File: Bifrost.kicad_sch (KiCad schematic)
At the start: 59 parts, among them J1 OIP, J2 Conn_01x03_Male, J3 Conn_01x03_Male, U1 RLP-50, U3 LMH6881

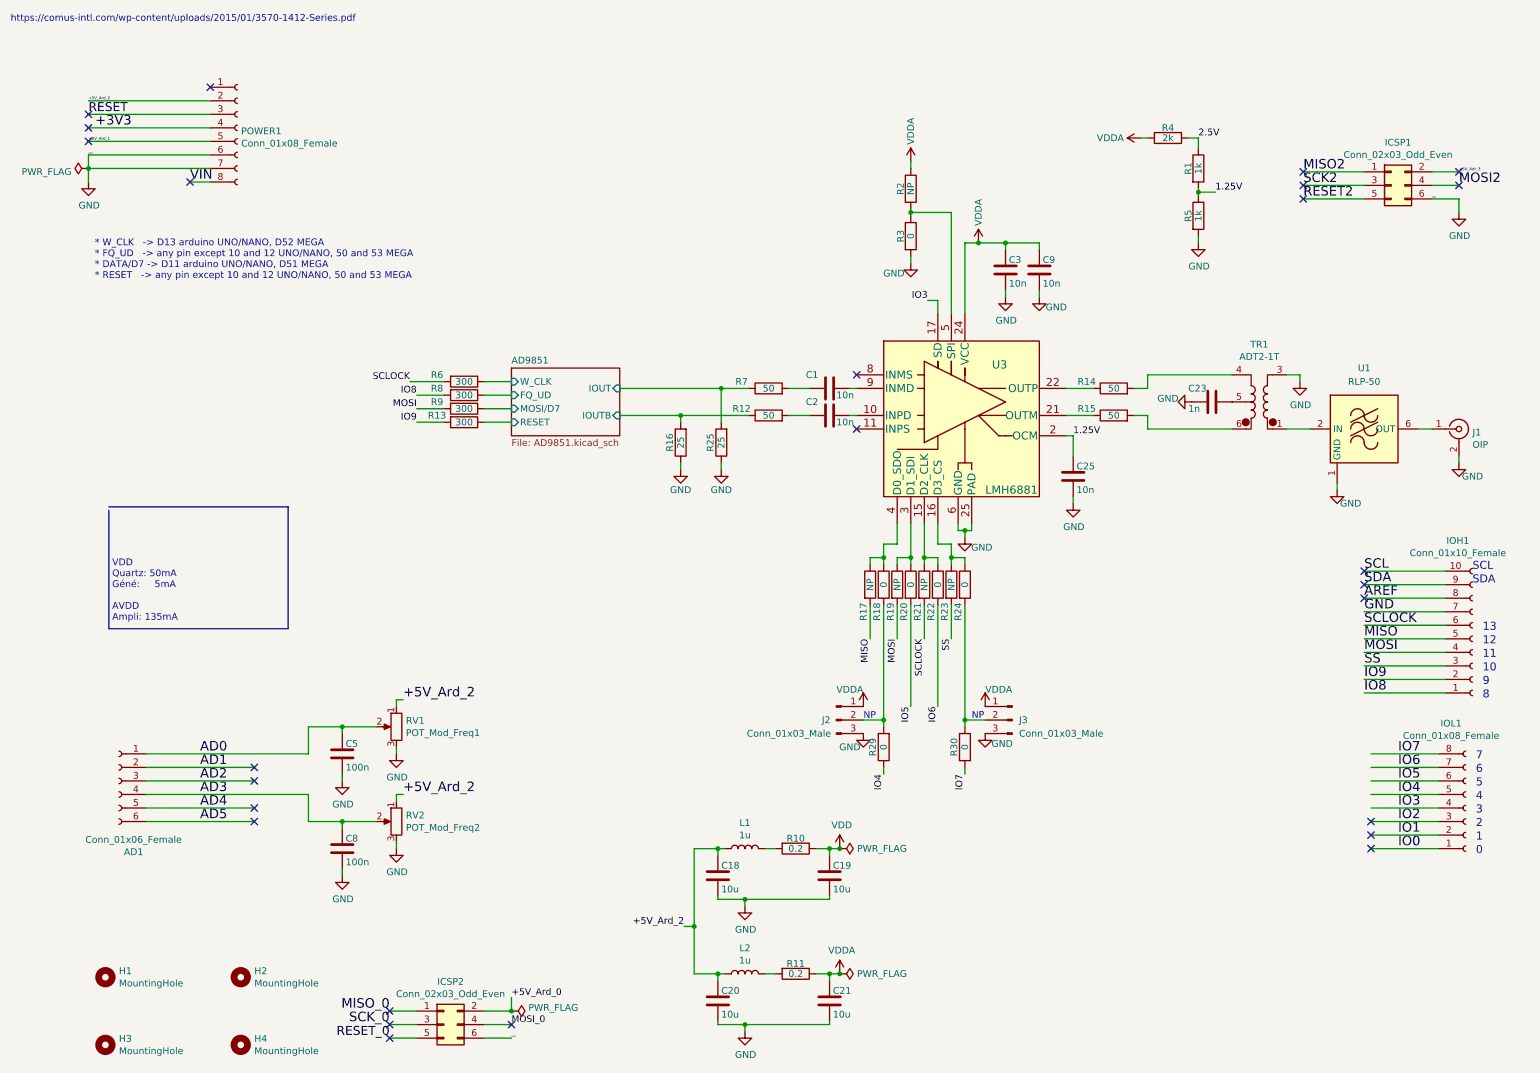
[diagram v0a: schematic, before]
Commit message: Replaced SPI selection resistors with a 6PDT (LMH6881 pins 3, 4, 5, 15, 16)
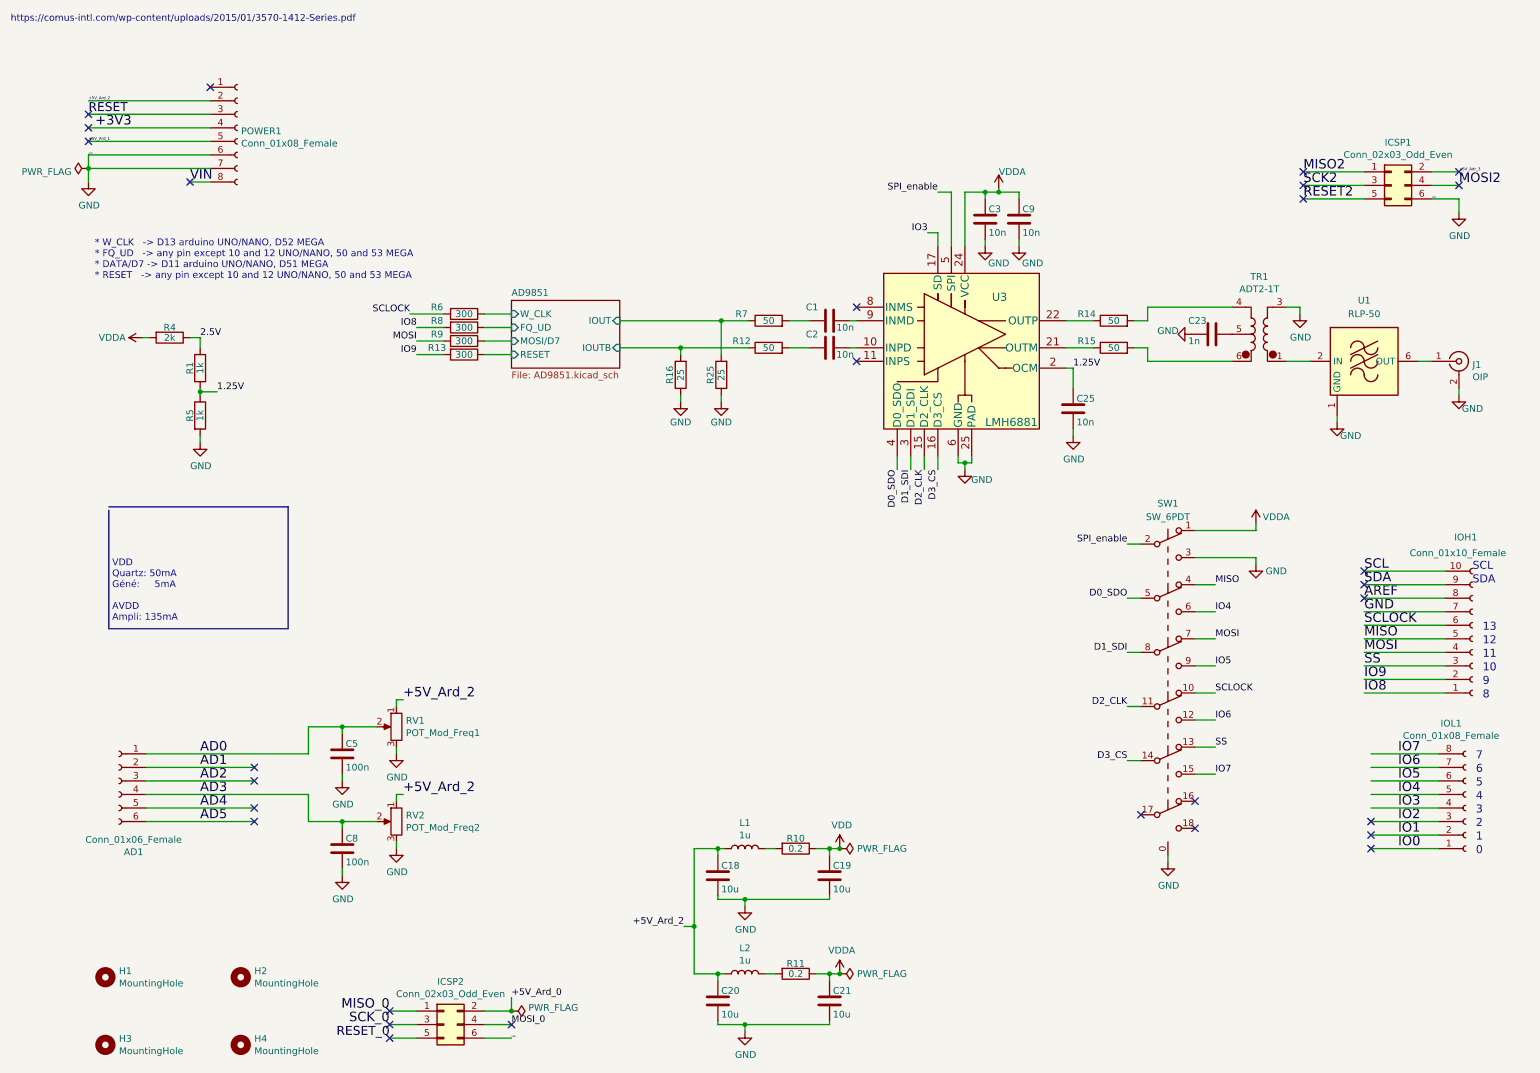
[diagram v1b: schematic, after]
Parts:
- removed J2, J3: Conn_01x03_Male, Connector_PinHeader_2.54mm:PinHeader_1x03_P2.54mm_Vertical, symbol Connector:Conn_01x03_Male
- removed R17, R19, R2, R21, R23: NP, Resistor_SMD:R_0603_1608Metric_Pad0.98x0.95mm_HandSolder, symbol Device:R
- removed R18, R20, R22, R24, R29, R3, R30: 0, Resistor_SMD:R_0603_1608Metric_Pad0.98x0.95mm_HandSolder, symbol Device:R
- added SW1: SW_6PDT, LibPersoNadj:SW_EG6201, symbol LibPersoNadj:SW_6PDT_Shield
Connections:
- net GND: now also SW1.0, SW1.3 (C)
- net IO4: now also SW1.6 (C)
- net IO5: now also SW1.9 (C)
- net IO6: now also SW1.12 (C)
- net IO7: now also SW1.15 (C)
- net MISO: now also SW1.4 (A)
- net MOSI: now also SW1.7 (A)
- net SCLOCK: now also SW1.10 (A)
- net SS: now also SW1.13 (A)
- net VCC: now also SW1.1 (A)
- net D2_CLK: now reaches U3.15 (D2_CLK)
- net D2_CLK: now also SW1.11 (B)
- net D3_CS: now reaches U3.16 (D3_CS)
- net D3_CS: now also SW1.14 (B)
- net D1_SDI: now reaches U3.3 (D1_SDI)
- net D1_SDI: now also SW1.8 (B)
- net D0_SDO: now reaches U3.4 (D0_SDO)
- net D0_SDO: now also SW1.5 (B)
- net SPI_enable: now reaches U3.5 (SPI)
- net SPI_enable: now also SW1.2 (B)
- no-connect marks 26 -> 29
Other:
- note removed: "NP"
- moved on the sheet: C1, C2, C23, C25, C3, C9, J1, R1, R12, R13, R14, R15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

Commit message: Implemented change on pcb Updated Schematics symbols to Kicad 7 standards (Female=>Socket...)
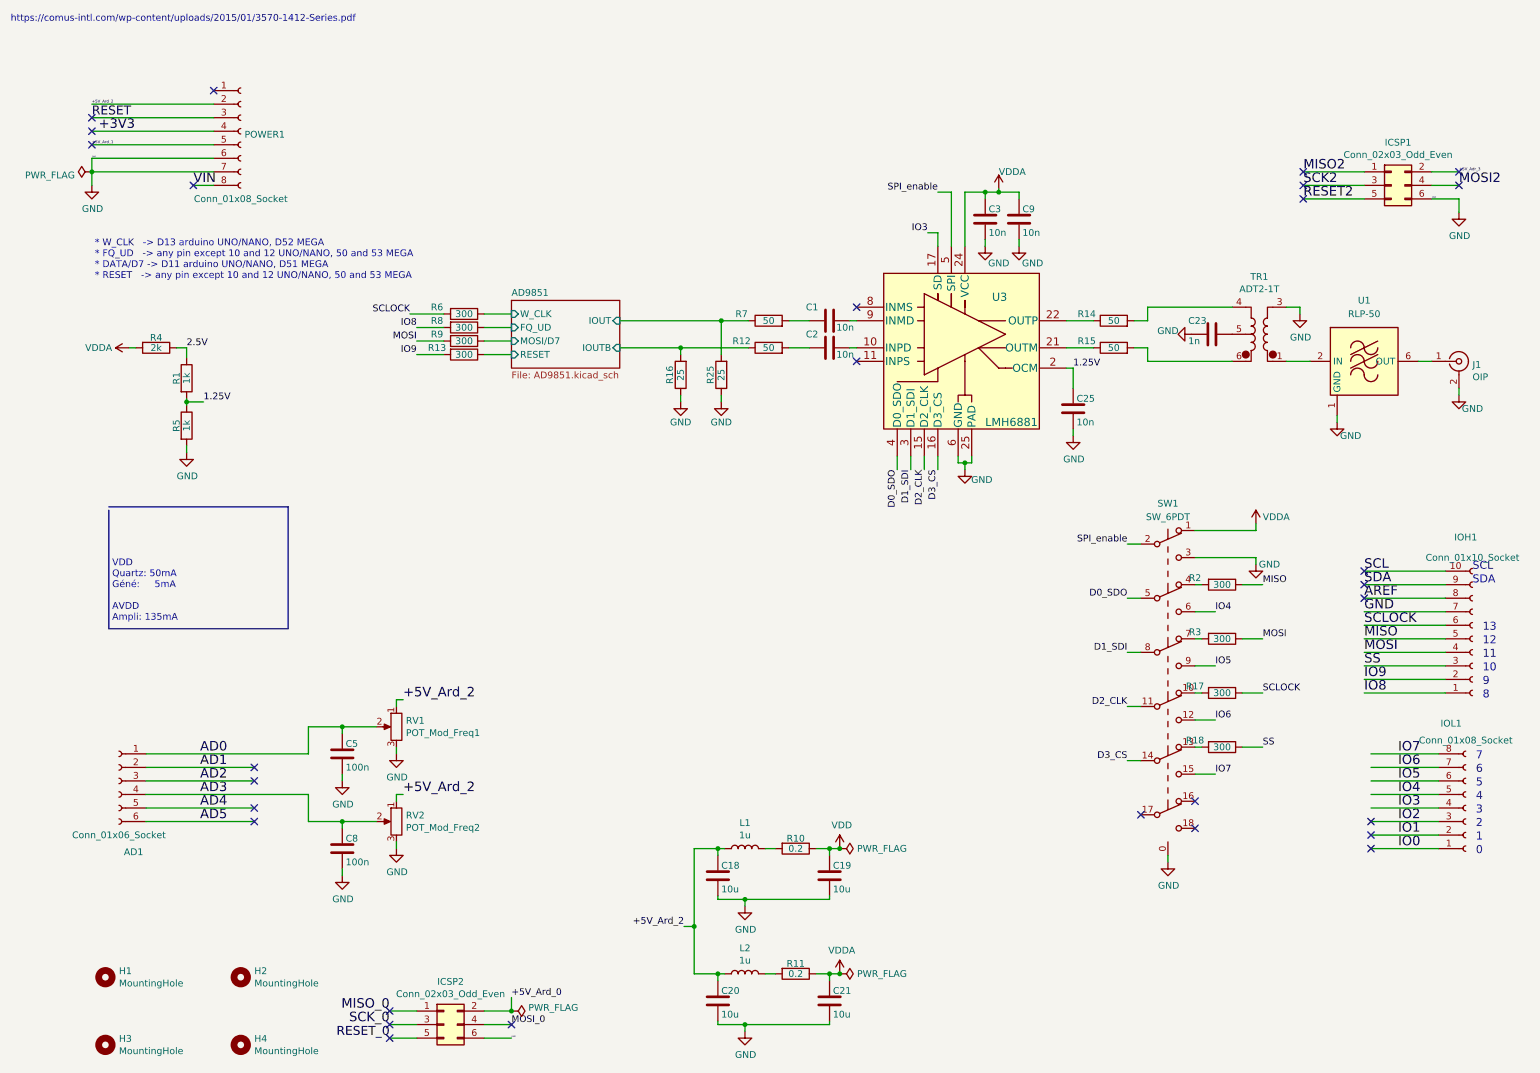
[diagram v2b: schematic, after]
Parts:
- added R17, R18, R2, R3: 300, Resistor_SMD:R_0603_1608Metric_Pad0.98x0.95mm_HandSolder, symbol Device:R
- AD1: value Conn_01x06_Female -> Conn_01x06_Socket; symbol Connector:Conn_01x06_Female -> Connector:Conn_01x06_Socket
- IOH1: value Conn_01x10_Female -> Conn_01x10_Socket; symbol Connector:Conn_01x10_Female -> Connector:Conn_01x10_Socket
- IOL1, POWER1: value Conn_01x08_Female -> Conn_01x08_Socket; symbol Connector:Conn_01x08_Female -> Connector:Conn_01x08_Socket
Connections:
- net MISO: now also R2.1; no longer SW1.4 (A)
- net MOSI: now also R3.1; no longer SW1.7 (A)
- net SCLOCK: now also R17.1; no longer SW1.10 (A)
- net SS: now also R18.1; no longer SW1.13 (A)
- new net: R2.2, SW1.4 (A)
- new net: R17.2, SW1.10 (A)
- new net: R18.2, SW1.13 (A)
- new net: R3.2, SW1.7 (A)
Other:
- moved on the sheet: POWER1, R1, R4, R5

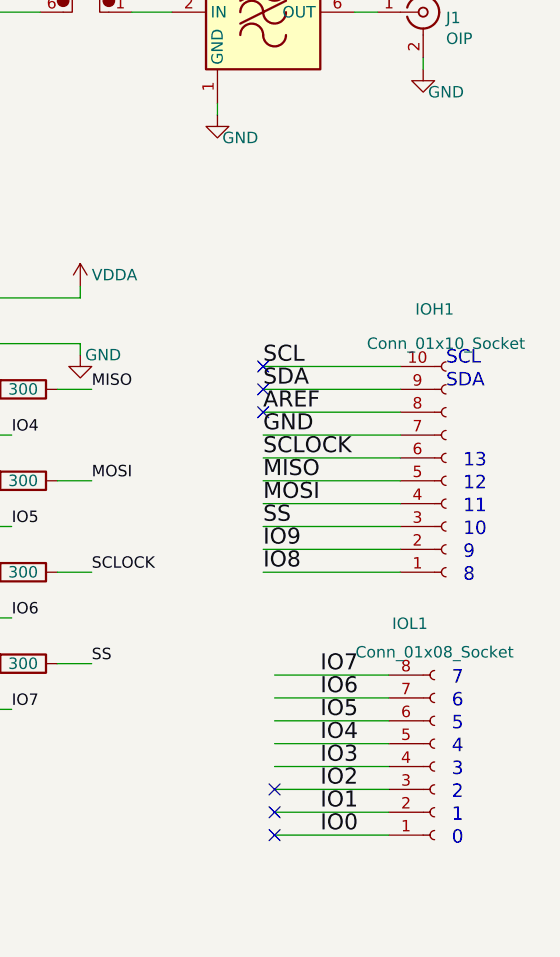
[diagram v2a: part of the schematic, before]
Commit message: Added TTL output
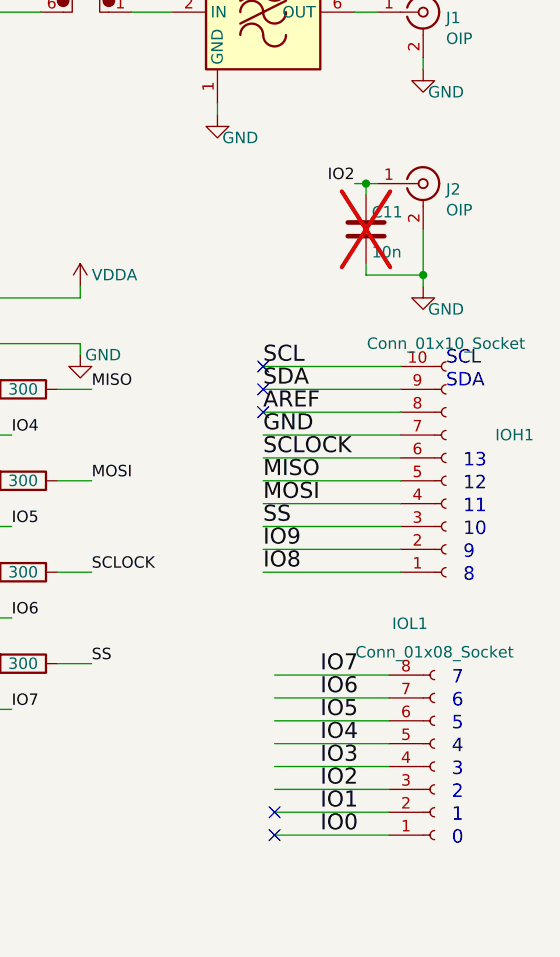
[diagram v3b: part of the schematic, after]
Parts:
- added C11: 10n, Capacitor_SMD:C_0603_1608Metric_Pad1.08x0.95mm_HandSolder, symbol Device:C
- added J2: OIP, Connector_Coaxial:SMA_Molex_73251-1153_EdgeMount_Horizontal, symbol Connector:Conn_Coaxial
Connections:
- net GND: now also C11.1, J2.2 (Ext)
- net IO2: now also C11.2, J2.1 (In)
- no-connect marks 29 -> 28
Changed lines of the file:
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@@
   (junction (at 153.67 157.48) (diameter 0) (color 0 0 0 0)
+  )
+  (junction (at 271.78 95.25) (diameter 0) (color 0 0 0 0)
+  )
+  (junction (at 265.43 85.09) (diameter 0) (color 0 0 0 0)
   )
   (junction (at 62.23 152.4) (diameter 0) (color 0 0 0 0)
@@
   (no_connect (at 254 110.49))
   (no_connect (at 45.72 152.4))
-  (no_connect (at 255.27 152.4))
   (no_connect (at 222.25 148.59))
   (no_connect (at 158.75 55.88))
@@
     (stroke (width 0) (type default))
   )
+  (wire (pts (xy 264.16 85.09) (xy 265.43 85.09))
+    (stroke (width 0) (type default))
+  )
   (wire (pts (xy 254 115.57) (xy 269.24 115.57))
     (stroke (width 0) (type default))
@@
     (stroke (width 0) (type default))
   )
+  (wire (pts (xy 271.78 90.17) (xy 271.78 95.25))
+    (stroke (width 0) (type default))
+  )
   (wire (pts (xy 179.07 85.09) (xy 180.34 85.09))
     (stroke (width 0) (type default))
@@
     (stroke (width 0) (type default))
   )
+  (wire (pts (xy 265.43 95.25) (xy 271.78 95.25))
+    (stroke (width 0) (type default))
+  )
   (wire (pts (xy 125.73 63.5) (xy 138.43 63.5))
     (stroke (width 0) (type default))
@@
     (stroke (width 0) (type default))
   )
+  (wire (pts (xy 265.43 93.98) (xy 265.43 95.25))
+    (stroke (width 0) (type default))
+  )
   (wire (pts (xy 76.2 59.69) (xy 81.28 59.69))
     (stroke (width 0) (type default))
@@
     (stroke (width 0) (type default))
   )
+  (wire (pts (xy 265.43 86.36) (xy 265.43 85.09))
+    (stroke (width 0) (type default))
+  )
   (wire (pts (xy 198.12 67.31) (xy 199.39 67.31))
     (stroke (width 0) (type default))
@@
     (stroke (width 0) (type default))
   )
+  (wire (pts (xy 265.43 85.09) (xy 266.7 85.09))
+    (stroke (width 0) (type default))
+  )
   (wire (pts (xy 33.02 73.025) (xy 33.02 73.66))
     (stroke (width 0) (type default))
   )
   (wire (pts (xy 132.715 157.48) (xy 132.715 158.75))
+    (stroke (width 0) (type default))
+  )
+  (wire (pts (xy 271.78 96.52) (xy 271.78 95.25))
     (stroke (width 0) (type default))
   )
@@
   (label "1.25V" (at 36.195 73.66 0) (fields_autoplaced)
     (effects (font (size 1.27 1.27)) (justify left bottom))
+  )
+  (label "IO2" (at 264.16 85.09 180) (fields_autoplaced)
+    (effects (font (size 1.27 1.27)) (justify right bottom))
   )
   (label "SPI_enable" (at 209.55 100.33 180) (fields_autoplaced)
@@
   (symbol (lib_id "Connector:Conn_01x10_Socket") (at 274.32 118.11 0) (mirror x) (unit 1)
     (in_bom yes) (on_board yes) (dnp no)
-    (property "Reference" "IOH1" (at 273.05 99.06 0)
+    (property "Reference" "IOH1" (at 281.94 113.03 0)
       (effects (font (size 1.27 1.27)))
     )
@@
     )
   )
+  (symbol (lib_id "power:GND") (at 271.78 96.52 0) (unit 1)
+    (in_bom yes) (on_board yes) (dnp no)
+    (property "Reference" "#PWR06" (at 271.78 102.87 0)
+      (effects (font (size 1.27 1.27)) hide)
+    )
+    (property "Value" "GND" (at 274.32 99.06 0)
+      (effects (font (size 1.27 1.27)))
+    )
+    (property "Footprint" "" (at 271.78 96.52 0)
+      (effects (font (size 1.27 1.27)) hide)
+    )
+    (property "Datasheet" "" (at 271.78 96.52 0)
+      (effects (font (size 1.27 1.27)) hide)
+    )
+    (pin "1")
+    (instances
+      (project "Bifrost"
+        (path "/2f8dfa45-14b0-4de4-b3b0-e7b73da81a0a"
+          (reference "#PWR06") (unit 1)
+        )
+      )
+    )
+  )
   (symbol (lib_id "RF_Filter:RLP-30") (at 254 66.04 0) (unit 1)
     (in_bom yes) (on_board yes) (dnp no) (fields_autoplaced)
@@
     )
   )
+  (symbol (lib_id "Device:C") (at 265.43 90.17 180) (unit 1)
+    (in_bom no) (on_board yes) (dnp yes)
+    (property "Reference" "C11" (at 266.065 88.265 0)
+      (effects (font (size 1.27 1.27)) (justify right))
+    )
+    (property "Value" "10n" (at 266.065 92.71 0)
+      (effects (font (size 1.27 1.27)) (justify right))
+    )
+    (property "Footprint" "Capacitor_SMD:C_0603_1608Metric_Pad1.08x0.95mm_HandSolder" (at 264.4648 86.36 0)
+      (effects (font (size 1.27 1.27)) hide)
+    )
+    (property "Datasheet" "~" (at 265.43 90.17 0)
+      (effects (font (size 1.27 1.27)) hide)
+    )
+    (pin "1")
+    (pin "2")
+    (instances
+      (project "Bifrost"
+        (path "/2f8dfa45-14b0-4de4-b3b0-e7b73da81a0a"
+          (reference "C11") (unit 1)
+        )
+      )
+    )
+  )
   (symbol (lib_id "Device:R") (at 133.35 68.58 180) (unit 1)
     (in_bom yes) (on_board yes) (dnp no)
@@
         )
       )
+    )
+  )
+  (symbol (lib_id "Connector:Conn_Coaxial") (at 271.78 85.09 0) (unit 1)
+    (in_bom yes) (on_board yes) (dnp no)
+    (property "Reference" "J2" (at 274.32 85.725 0)
+      (effects (font (size 1.27 1.27)) (justify left))
+    )
+    (property "Value" "OIP" (at 274.32 88.0364 0)
+      (effects (font (size 1.27 1.27)) (justify left))
+    )
+    (property "Footprint" "Connector_Coaxial:SMA_Molex_73251-1153_EdgeMount_Horizontal" (at 271.78 85.09 0)
+      (effects (font (size 1.27 1.27)) hide)
+    )
+    (property "Datasheet" " ~" (at 271.78 85.09 0)
+      (effects (font (size 1.27 1.27)) hide)
+    )
+    (pin "1")
+    (pin "2")
+    (instances
+      (project "Bifrost"
+        (path "/2f8dfa45-14b0-4de4-b3b0-e7b73da81a0a"
+          (reference "J2") (unit 1)
+        )
+      )

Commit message: As impemented v2
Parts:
- C18, C19, C20, C21: footprint Capacitor_SMD:C_0603_1608Metric_Pad1.08x0.95mm_HandSolder -> Capacitor_SMD:C_1206_3216Metric_Pad1.33x1.80mm_HandSolder
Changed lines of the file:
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@@
       (effects (font (size 1.27 1.27)) (justify right))
     )
-    (property "Footprint" "Capacitor_SMD:C_0603_1608Metric_Pad1.08x0.95mm_HandSolder" (at 131.7498 182.245 0)
+    (property "Footprint" "Capacitor_SMD:C_1206_3216Metric_Pad1.33x1.80mm_HandSolder" (at 131.7498 182.245 0)
       (effects (font (size 1.27 1.27)) hide)
     )
@@
       (effects (font (size 1.27 1.27)) (justify right))
     )
-    (property "Footprint" "Capacitor_SMD:C_0603_1608Metric_Pad1.08x0.95mm_HandSolder" (at 152.7048 182.245 0)
+    (property "Footprint" "Capacitor_SMD:C_1206_3216Metric_Pad1.33x1.80mm_HandSolder" (at 152.7048 182.245 0)
       (effects (font (size 1.27 1.27)) hide)
     )
@@
       (effects (font (size 1.27 1.27)) (justify right))
     )
-    (property "Footprint" "Capacitor_SMD:C_0603_1608Metric_Pad1.08x0.95mm_HandSolder" (at 131.7498 158.75 0)
+    (property "Footprint" "Capacitor_SMD:C_1206_3216Metric_Pad1.33x1.80mm_HandSolder" (at 131.7498 158.75 0)
       (effects (font (size 1.27 1.27)) hide)
     )
@@
       (effects (font (size 1.27 1.27)) (justify right))
     )
-    (property "Footprint" "Capacitor_SMD:C_0603_1608Metric_Pad1.08x0.95mm_HandSolder" (at 152.7048 158.75 0)
+    (property "Footprint" "Capacitor_SMD:C_1206_3216Metric_Pad1.33x1.80mm_HandSolder" (at 152.7048 158.75 0)
       (effects (font (size 1.27 1.27)) hide)
     )
